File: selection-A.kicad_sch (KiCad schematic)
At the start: 4 parts, among them U10 SN74LVC1G32DBVR, U7 SN74LS08N, U9 SN74LS08N

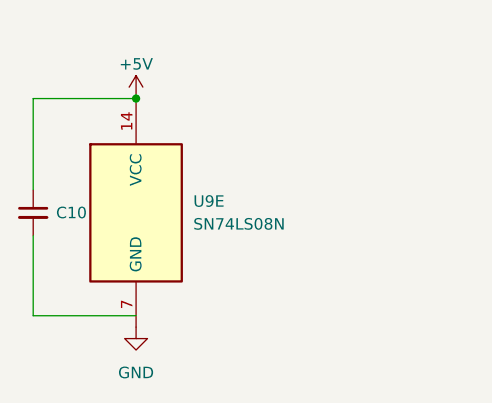
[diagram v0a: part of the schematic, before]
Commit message: fix: fixed link of capas
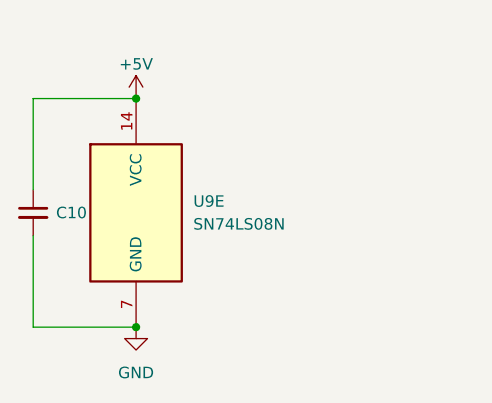
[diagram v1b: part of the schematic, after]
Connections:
- net GND: now also C10.2
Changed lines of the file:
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@@
+	)
+	(junction
+		(at 54.61 154.94)
+		(diameter 0)
+		(color 0 0 0 0)
 	)
 	(junction
@@
 	(wire
 		(pts
-			(xy 54.61 153.67) (xy 43.18 153.67)
+			(xy 43.18 154.94) (xy 54.61 154.94)
+		)
+		(stroke
+			(width 0)
+			(type default)
+		)
+	)
+	(wire
+		(pts
+			(xy 43.18 144.78) (xy 43.18 154.94)
 		)
 		(stroke
@@
 		)
 		(stroke
-			(width 0)
-			(type default)
-		)
-	)
-	(wire
-		(pts
-			(xy 43.18 153.67) (xy 43.18 144.78)
-		)
-		(stroke

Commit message: feat: updated references
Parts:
- C10: value C_Small -> CC0603KRX7R9BB104
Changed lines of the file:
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@@
 			)
 		)
-		(property "Value" "C_Small"
+		(property "Value" "CC0603KRX7R9BB104"
 			(at 45.72 143.5162 0)
 			(hide yes)

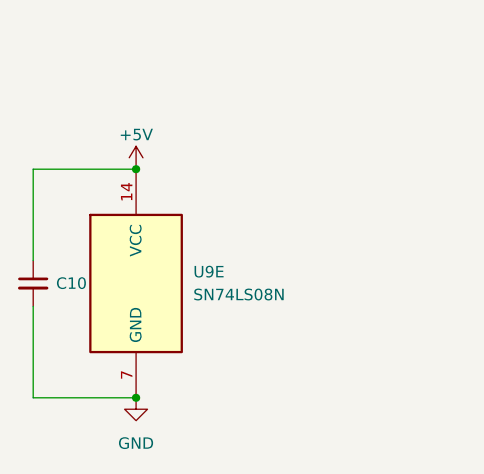
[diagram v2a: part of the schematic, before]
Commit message: Remove capacitors + change R and C footprints + finish PCB routing
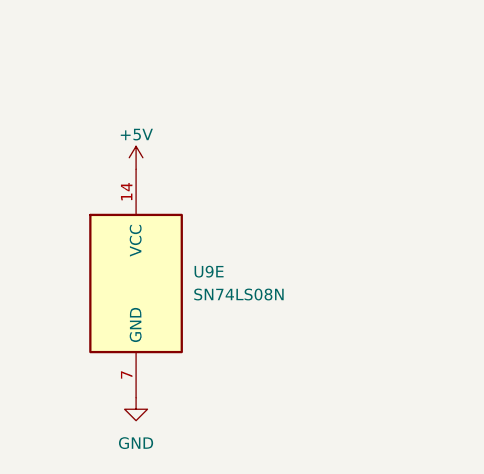
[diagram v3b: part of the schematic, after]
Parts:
- removed C10: CC0603KRX7R9BB104, Capacitor_SMD:C_0603_1608Metric_Pad1.08x0.95mm_HandSolder, symbol Device:C_Small
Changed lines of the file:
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@@
-	)
-	(junction
-		(at 54.61 129.54)
-		(diameter 0)
-		(color 0 0 0 0)
-	)
-	(junction
-		(at 54.61 154.94)
-		(diameter 0)
-		(color 0 0 0 0)
 	)
 	(junction
@@
 	(wire
 		(pts
-			(xy 54.61 129.54) (xy 43.18 129.54)
-		)
-		(stroke
-			(width 0)
-			(type default)
-		)
-	)
-	(wire
-		(pts
 			(xy 91.44 43.18) (xy 96.52 43.18)
 		)
@@
 	(wire
 		(pts
-			(xy 43.18 154.94) (xy 54.61 154.94)
-		)
-		(stroke
-			(width 0)
-			(type default)
-		)
-	)
-	(wire
-		(pts
-			(xy 43.18 144.78) (xy 43.18 154.94)
-		)
-		(stroke
-			(width 0)
-			(type default)
-		)
-	)
-	(wire
-		(pts
 			(xy 124.46 106.68) (xy 128.27 106.68)
 		)
@@
 		(pts
 			(xy 143.51 90.17) (xy 147.32 90.17)
-		)
-		(stroke
-			(width 0)
-			(type default)
-		)
-	)
-	(wire
-		(pts
-			(xy 43.18 129.54) (xy 43.18 139.7)
 		)
 		(stroke
@@
 				)
 			)
-		)
-	)
-	(symbol
-		(lib_id "Device:C_Small")
-		(at 43.18 142.24 0)
-		(unit 1)
-		(body_style 1)
-		(exclude_from_sim no)
-		(in_bom yes)
-		(on_board yes)
-		(in_pos_files yes)
-		(dnp no)
-		(fields_autoplaced yes)
-		(property "Reference" "C10"
-			(at 45.72 142.2462 0)
-			(show_name no)
-			(do_not_autoplace no)
-			(effects
-				(font
-					(size 1.27 1.27)
-				)
-				(justify left)
-			)
-		)
-		(property "Value" "CC0603KRX7R9BB104"
-			(at 45.72 143.5162 0)
-			(hide yes)
-			(show_name no)
-			(do_not_autoplace no)
-			(effects
-				(font
-					(size 1.27 1.27)
-				)
-				(justify left)
-			)
-		)
-		(property "Footprint" "Capacitor_SMD:C_0603_1608Metric_Pad1.08x0.95mm_HandSolder"
-			(at 43.18 142.24 0)
-			(hide yes)
-			(show_name no)
-			(do_not_autoplace no)
-			(effects
-				(font
-					(size 1.27 1.27)
-				)
-			)
-		)
-		(property "Datasheet" ""
-			(at 43.18 142.24 0)
-			(hide yes)
-			(show_name no)
-			(do_not_autoplace no)
-			(effects
-				(font
-					(size 1.27 1.27)
-				)
-			)
-		)
-		(property "Description" "Unpolarized capacitor, small symbol"
-			(at 43.18 142.24 0)
-			(hide yes)
-			(show_name no)
-			(do_not_autoplace no)
-			(effects
-				(font
-					(size 1.27 1.27)
-				)
-			)
-		)
-		(pin "2"
-		)
-		(pin "1"
-		)
-		(instances
-			(project "alu"
-				(path "/4987240f-8890-46b8-b8e9-0d60580cb205/30c1ae8d-c878-40aa-ace0-371f489a4d3c"
-					(reference "C10")
-					(unit 1)
-				)
-			)

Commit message: fix: reput capas -- where is my gift?
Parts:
- added C10: C_Small, Capacitor_SMD:C_0603_1608Metric, symbol Device:C_Small
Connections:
- net +5V: now also C10.1
- net GND: now also C10.2

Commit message: feat: added point_tests + fixed wrong footprint for switch + added anime girl
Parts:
- added OUT_SEL_ADD_A0, OUT_SEL_ADD_A1, OUT_SEL_ADD_A2, OUT_SEL_ADD_A3, OUT_SEL_MUL_A0, OUT_SEL_MUL_A1: TestPoint, TestPoint:TestPoint_THTPad_D1.0mm_Drill0.5mm, symbol Connector:TestPoint
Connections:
- net OUT_ADD_A0: now also OUT_SEL_ADD_A0.1
- net OUT_ADD_A1: now also OUT_SEL_ADD_A1.1
- net OUT_ADD_A2: now also OUT_SEL_ADD_A2.1
- net OUT_ADD_A3: now also OUT_SEL_ADD_A3.1
- net OUT_MUL_A0: now also OUT_SEL_MUL_A0.1
- net OUT_MUL_A1: now also OUT_SEL_MUL_A1.1

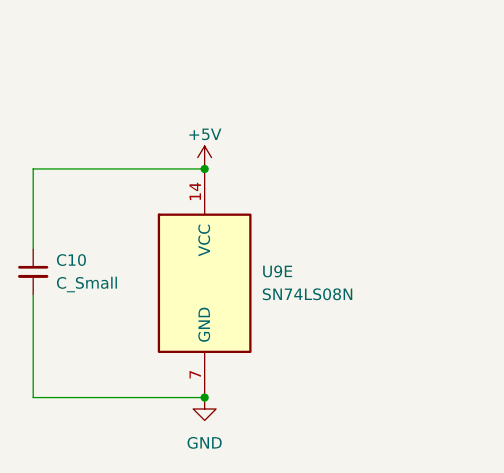
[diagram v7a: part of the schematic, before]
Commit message: chore: changed R and C ref to passive value
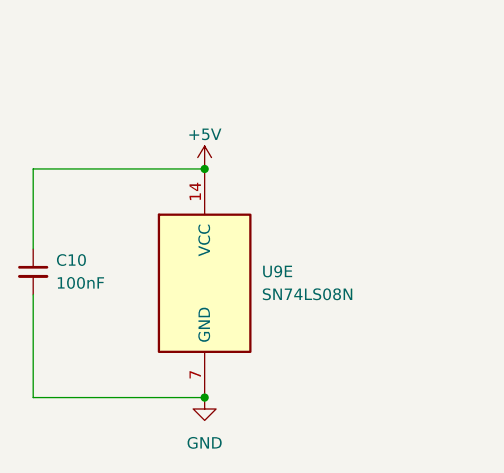
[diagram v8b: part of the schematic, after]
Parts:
- C10: value C_Small -> 100nF
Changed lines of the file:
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@@
 			)
 		)
-		(property "Value" "C_Small"
+		(property "Value" "100nF"
 			(at 38.1 142.2462 0)
 			(effects
